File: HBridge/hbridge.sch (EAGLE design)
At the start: 4 parts, among them IC1 337T, Q1 IRF9530, T1 2N2222

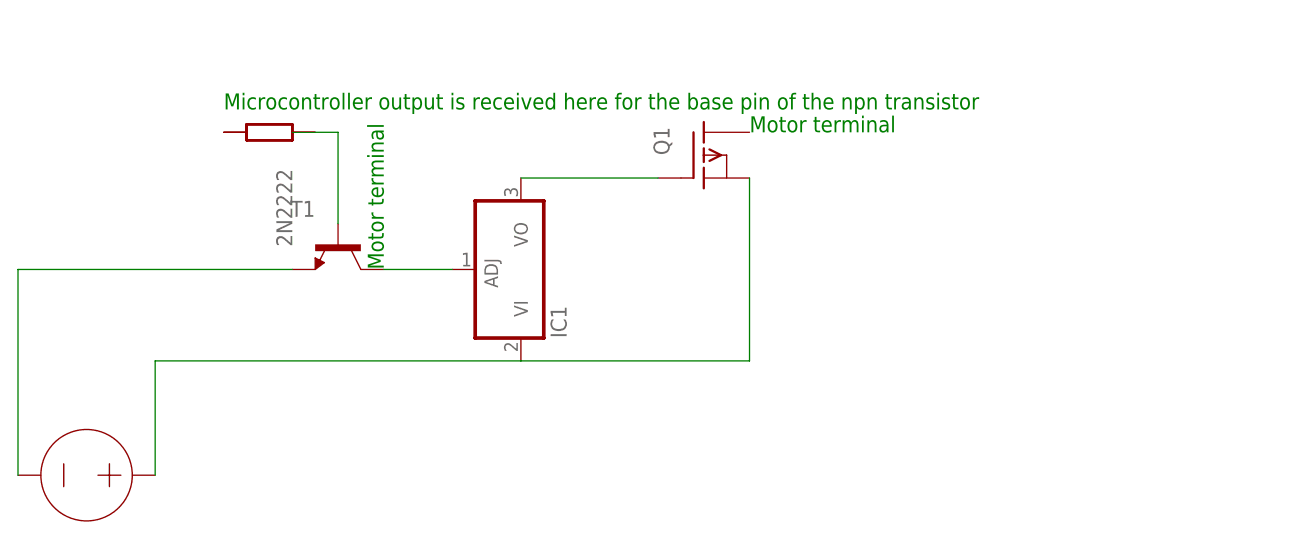
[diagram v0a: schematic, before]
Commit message: Updated Eagle files
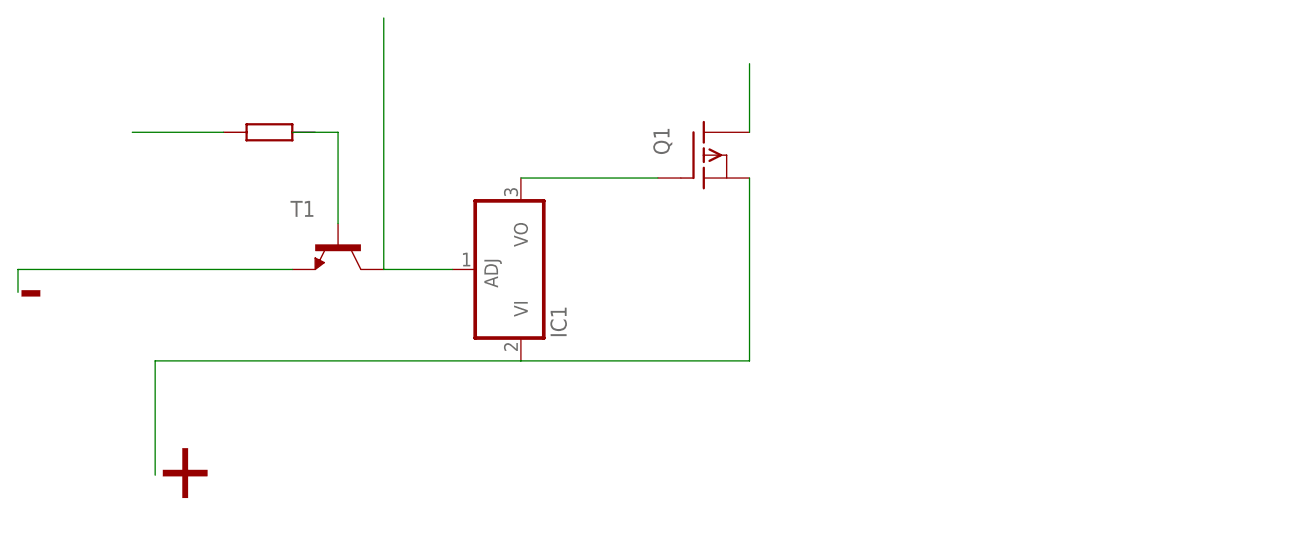
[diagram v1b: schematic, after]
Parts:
- removed V1: 0V, ngspice-simulation:VOLTAGE
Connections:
- new net N$4: Q1.D
- net N$1: no longer V1.+
- net T1_E: no longer V1.-
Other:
- note added: "+"
- note added: "-"
- note removed: "Microcontroller output is received here for the base pin of the npn transistor"
- note removed: "Motor terminal"
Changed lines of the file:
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@@
 <part name="IC1" library="linear" library_urn="urn:adsk.eagle:library:262" deviceset="*337" device="T" package3d_urn="urn:adsk.eagle:package:16414/1"/>
 <part name="T1" library="transistor" library_urn="urn:adsk.eagle:library:402" deviceset="2N2222" device="" package3d_urn="urn:adsk.eagle:package:29892/2"/>
-<part name="V1" library="ngspice-simulation" library_urn="urn:adsk.eagle:library:527439" deviceset="VOLTAGE" device="" value="0V"/>
 <part name="R1" library="docu-dummy" library_urn="urn:adsk.eagle:library:215" deviceset="R" device=""/>
-<part name="RB" library="docu-dummy" library_urn="urn:adsk.eagle:library:215" deviceset="R" device=""/>
 </parts>
 <sheets>
 <sheet>
 <plain>
-<text x="-66.04" y="187.96" size="1.778" layer="91">Motor terminal</text>
-<text x="-106.68" y="172.72" size="1.778" layer="91" rot="R90">Motor terminal</text>
-<text x="-124.46" y="190.5" size="1.778" layer="91">Microcontroller output is received here for the base pin of the npn transistor </text>
+<text x="-132.08" y="147.32" size="6.4516" layer="94">+</text>
+<text x="-147.32" y="167.64" size="6.4516" layer="94">-</text>
 </plain>
 <instances>
@@
 <instance part="T1" gate="G$1" x="-111.76" y="175.26" smashed="yes" rot="R270">
 <attribute name="NAME" x="-114.3" y="180.34" size="1.778" layer="95" rot="R180"/>
-<attribute name="VALUE" x="-116.84" y="175.26" size="1.778" layer="96" rot="R90"/>
 </instance>
-<instance part="V1" gate="G$1" x="-139.7" y="149.86" smashed="yes" rot="R270"/>
 <instance part="R1" gate="G$1" x="-119.38" y="187.96" smashed="yes"/>
-<instance part="RB" gate="G$1" x="-119.38" y="187.96" smashed="yes"/>
 </instances>
 <busses>
@@
 <pinref part="IC1" gate="A1" pin="ADJ"/>
 <wire x1="-106.68" y1="172.72" x2="-99.06" y2="172.72" width="0.1524" layer="91"/>
+<wire x1="-106.68" y1="172.72" x2="-106.68" y2="200.66" width="0.1524" layer="91"/>
 </segment>
 </net>
@@
 <segment>
 <pinref part="T1" gate="G$1" pin="E"/>
-<pinref part="V1" gate="G$1" pin="-"/>
-<wire x1="-147.32" y1="149.86" x2="-147.32" y2="172.72" width="0.1524" layer="91"/>
+<wire x1="-147.32" y1="170.18" x2="-147.32" y2="172.72" width="0.1524" layer="91"/>
 <wire x1="-147.32" y1="172.72" x2="-116.84" y2="172.72" width="0.1524" layer="91"/>
 </segment>
@@
 <pinref part="IC1" gate="A1" pin="VI"/>
 <wire x1="-91.44" y1="162.56" x2="-132.08" y2="162.56" width="0.1524" layer="91"/>
-<pinref part="V1" gate="G$1" pin="+"/>
 <wire x1="-132.08" y1="162.56" x2="-132.08" y2="149.86" width="0.1524" layer="91"/>
 <pinref part="Q1" gate="G$1" pin="S"/>
@@
 <wire x1="-111.76" y1="177.8" x2="-111.76" y2="187.96" width="0.1524" layer="91"/>
 <wire x1="-111.76" y1="187.96" x2="-116.84" y2="187.96" width="0.1524" layer="91"/>
+</segment>
+</net>
+<net name="N$4" class="0">
+<segment>
+<pinref part="Q1" gate="G$1" pin="D"/>
+<wire x1="-66.04" y1="187.96" x2="-66.04" y2="195.58" width="0.1524" layer="91"/>
+</segment>
+</net>
+<net name="N$5" class="0">
+<segment>
+<wire x1="-124.46" y1="187.96" x2="-134.62" y2="187.96" width="0.1524" layer="91"/>
 </segment>
 </net>
@@
 packages will not be understood (or retained) with this version.
 </note>
-<note version="8.4" severity="warning">
-Since Version 8.4, EAGLE supports properties for SPICE simulation.
-Probes in schematics and SPICE mapping objects found in parts and library devices
-will not be understood with this version. Update EAGLE to the latest version
-for full support of SPICE simulation.
-</note>
 </compatibility>
